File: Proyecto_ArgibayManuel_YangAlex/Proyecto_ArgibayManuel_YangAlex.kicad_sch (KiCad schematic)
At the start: 29 parts, among them J1 Con_1x3, J2 Con_1x2, J3 Con_1x3, J4 Conn_01x03_Pin, J5 Conn_01x06, SW1 SW_Push, SW2 SW_Push, SW3 SW_Push, SW4 SW_Push, U1 PIC18F258-I_SO, U2 HDC2010YPAR, U3 LT1716IS5TRMPBF, U4 LT1716IS5TRMPBF, U5 TXS0108EPW, Y1 Crystal

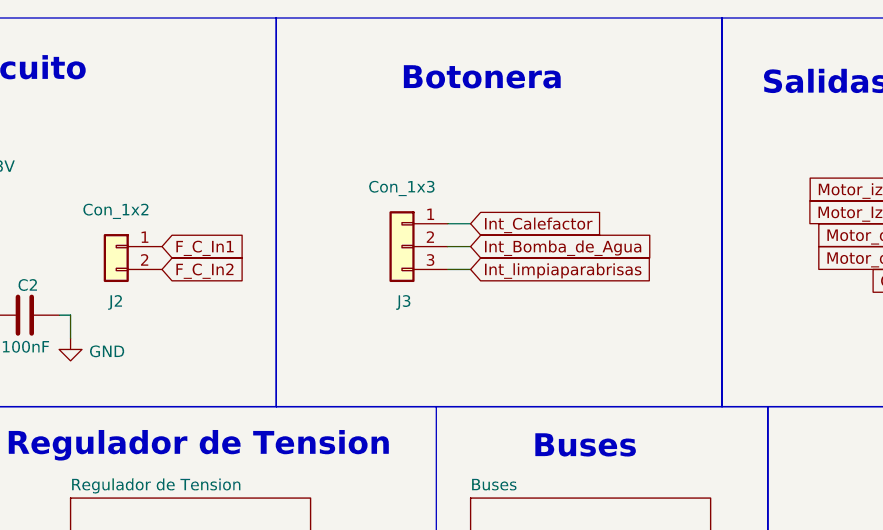
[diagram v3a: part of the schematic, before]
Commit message: Cambio layout (faltan agregar vías y reorganizar con la capa BOTTOM)
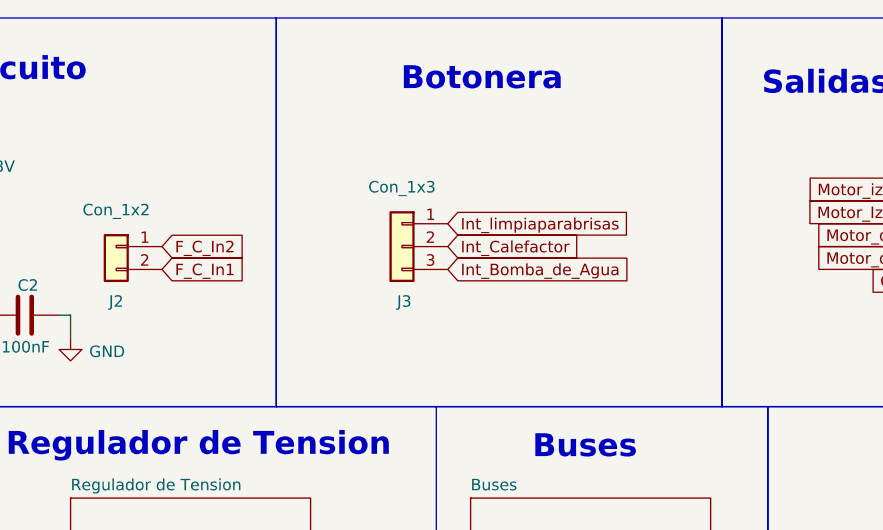
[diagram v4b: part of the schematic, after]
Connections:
- net F_C_In1: now also J2.2 (Pin_2); no longer J2.1 (Pin_1)
- net F_C_In2: now also J2.1 (Pin_1); no longer J2.2 (Pin_2)
- net Int_Bomba_de_Agua: now also J3.3 (Pin_3); no longer J3.2 (Pin_2)
- net Int_Calefactor: now also J3.2 (Pin_2); no longer J3.1 (Pin_1)
- net Int_limpiaparabrisas: now also J3.1 (Pin_1); no longer J3.3 (Pin_3)

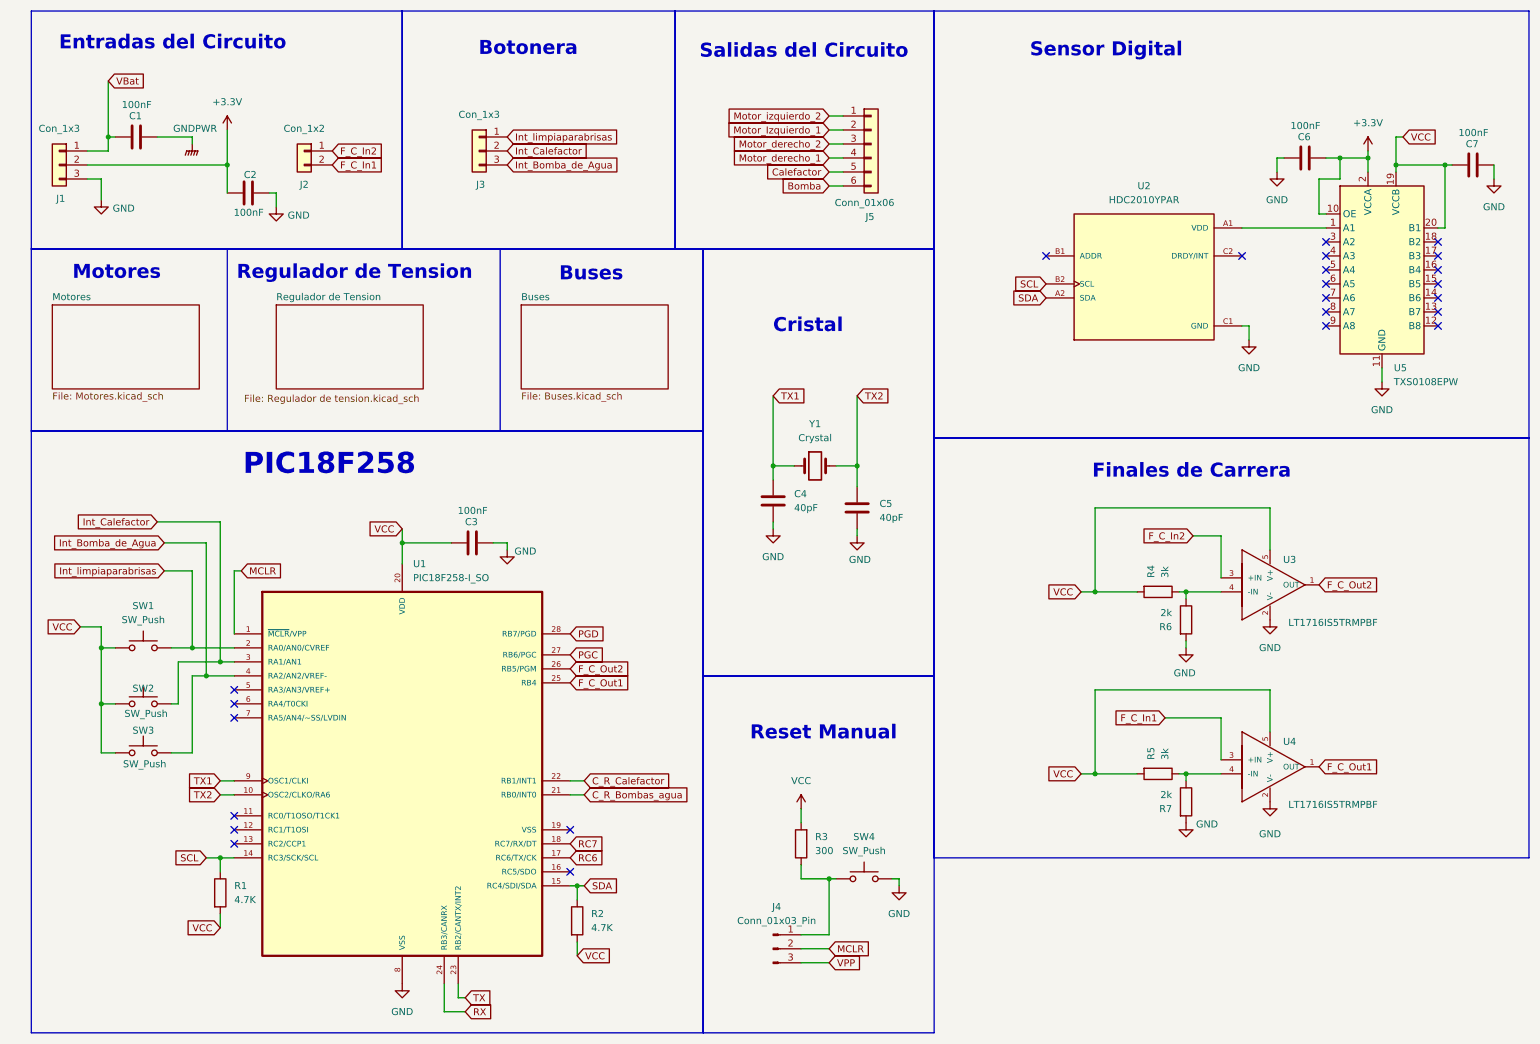
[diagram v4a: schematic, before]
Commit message: Termino layout (faltan acomodar etiquetas en la pcb))
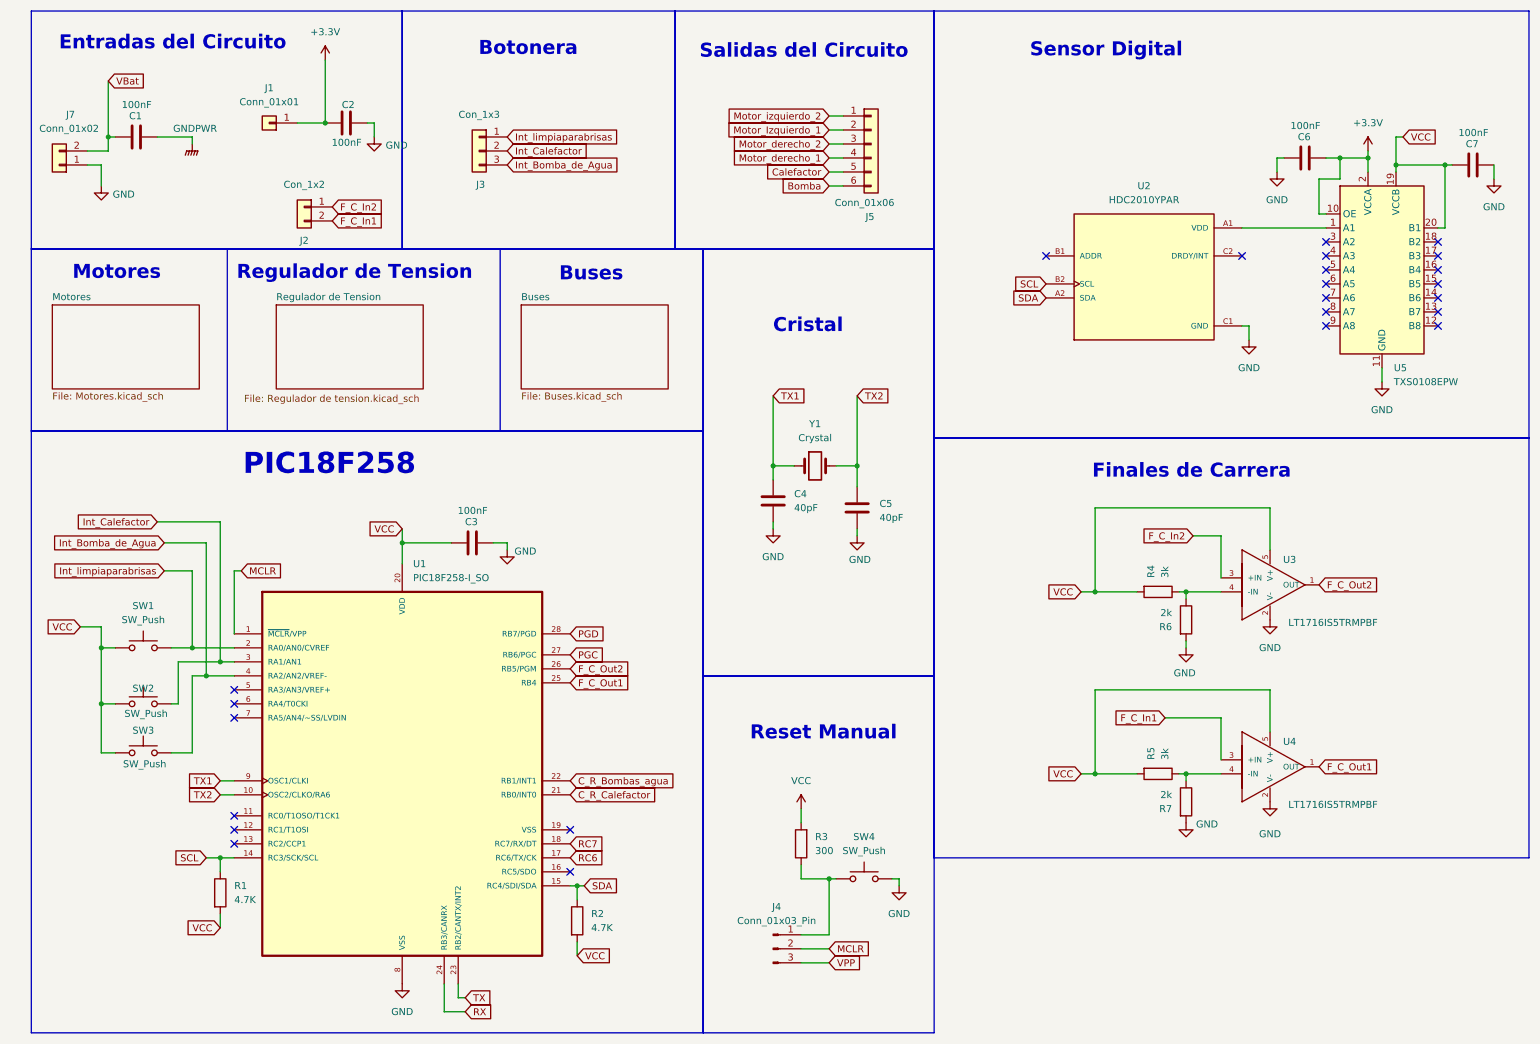
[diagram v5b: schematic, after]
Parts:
- removed J1: Con_1x3, Connector_PinHeader_2.54mm:PinHeader_1x03_P2.54mm_Vertical, symbol Connector_Generic:Conn_01x03
- added J1: Conn_01x01, Connector_PinHeader_2.54mm:PinHeader_1x01_P2.54mm_Vertical, symbol Connector_Generic:Conn_01x01
- added J7: Conn_01x02, Connector_PinHeader_2.54mm:PinHeader_1x02_P2.54mm_Vertical, symbol Connector_Generic:Conn_01x02
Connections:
- net +3.3V: now also J1.1 (Pin_1)
- net C_R_Bombas_agua: now also U1.22 (RB1/INT1); no longer U1.21 (RB0/INT0)
- net C_R_Calefactor: now also U1.21 (RB0/INT0); no longer U1.22 (RB1/INT1)
- net GND: now also J7.1 (Pin_1)
- net VBat: now also J7.2 (Pin_2)
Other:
- moved on the sheet: C2, J2

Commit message: Cambio de presentacion(esquematico,consumo,layout), minimas correciones en el esquematico
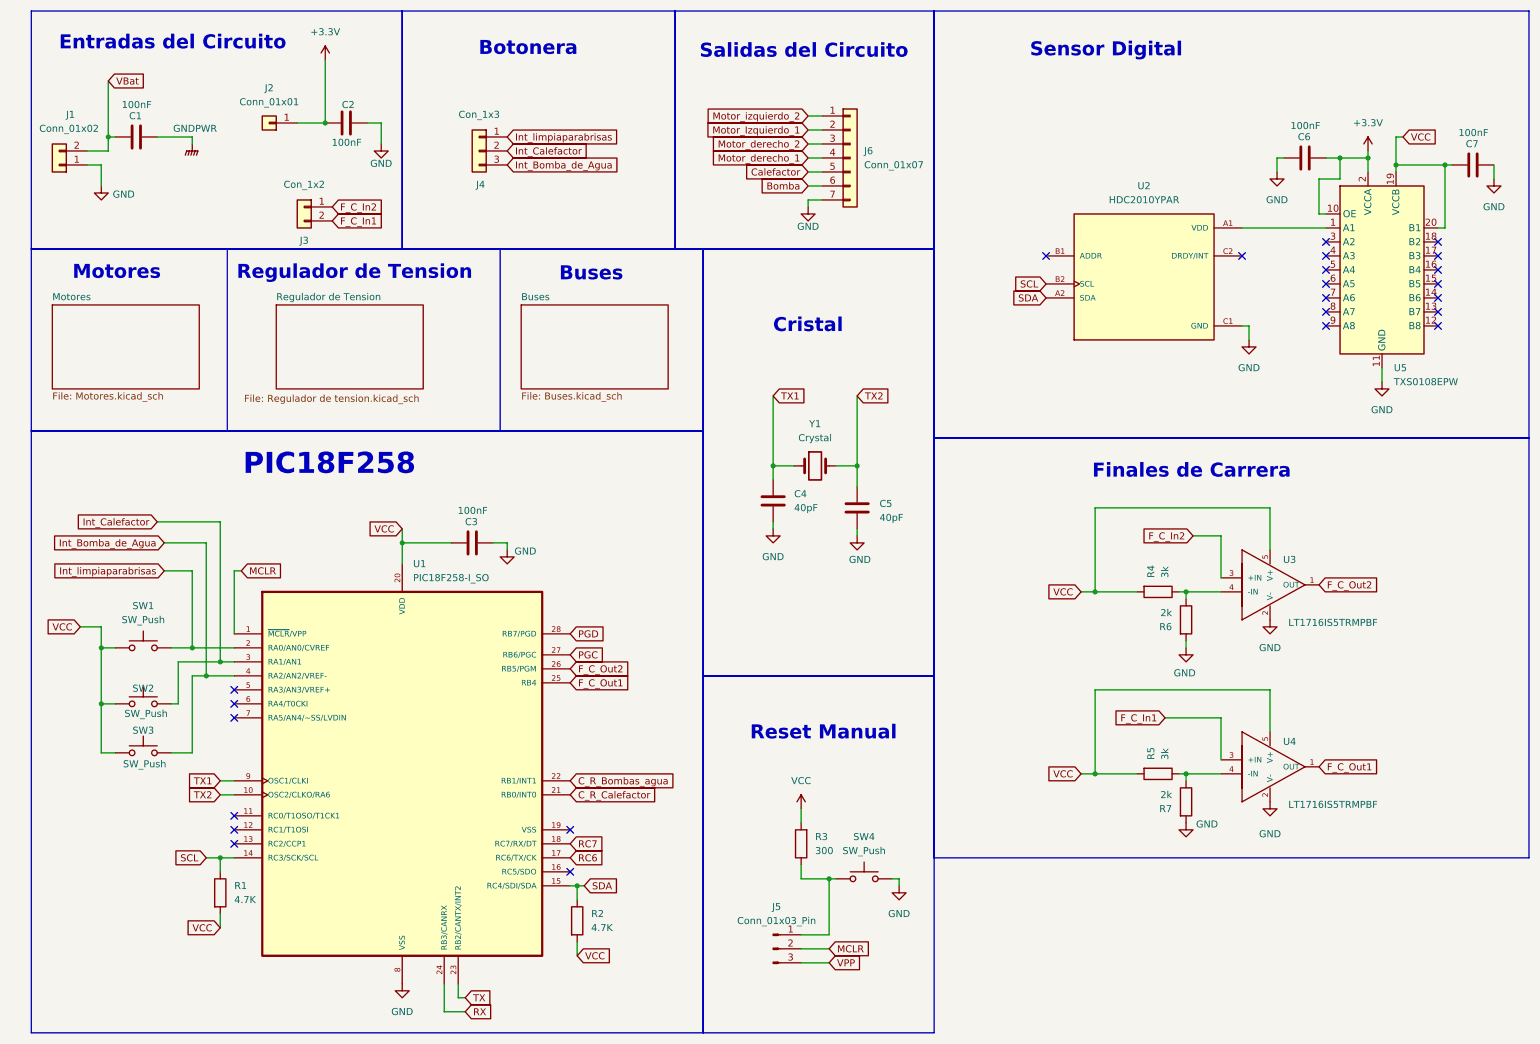
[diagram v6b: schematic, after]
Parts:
- removed J5: Conn_01x06, TerminalBlock_Phoenix:TerminalBlock_Phoenix_MKDS-1,5-6_1x06_P5.00mm_Horizontal, symbol Connector_Generic:Conn_01x06
- added J6: Conn_01x07, TerminalBlock_Phoenix:TerminalBlock_Phoenix_MKDS-1,5-7_1x07_P5.00mm_Horizontal, symbol Connector_Generic:Conn_01x07
- renumbered J7 to J1, J1 to J2, J2 to J3, J3 to J4, J4 to J5
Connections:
- net Bomba: now also J6.6 (Pin_6)
- net Calefactor: now also J6.5 (Pin_5)
- net GND: now also J6.7 (Pin_7)
- net Motor_Izquierdo_1: now also J6.2 (Pin_2)
- net Motor_derecho_1: now also J6.4 (Pin_4)
- net Motor_derecho_2: now also J6.3 (Pin_3)
- net Motor_izquierdo_2: now also J6.1 (Pin_1)

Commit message: Agrego cambios
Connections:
- net Bomba: now also J6.5 (Pin_5); no longer J6.6 (Pin_6)
- net Calefactor: now also J6.6 (Pin_6); no longer J6.5 (Pin_5)
- net GND: no longer J1.1 (Pin_1), J6.7 (Pin_7)
- net GNDPWR: now also J1.1 (Pin_1), J6.7 (Pin_7)
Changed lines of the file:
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@@
 	(wire
 		(pts
-			(xy 153.67 41.91) (xy 156.21 41.91)
+			(xy 260.35 35.56) (xy 260.35 40.64)
 		)
 		(stroke
@@
 		)
 	)
-	(wire
+	(polyline
 		(pts
-			(xy 260.35 35.56) (xy 260.35 40.64)
+			(xy 97.79 55.88) (xy 97.79 88.9)
 		)
 		(stroke
@@
 		)
 	)
-	(polyline
+	(wire
 		(pts
-			(xy 97.79 55.88) (xy 97.79 88.9)
+			(xy 153.67 41.91) (xy 156.21 41.91)
 		)
 		(stroke
@@
 	(wire
 		(pts
+			(xy 153.67 44.45) (xy 156.21 44.45)
+		)
+		(stroke
+			(width 0)
+			(type default)
+		)
+	)
+	(wire
+		(pts
 			(xy 44.45 133.35) (xy 49.53 133.35)
 		)
@@
 	(wire
 		(pts
-			(xy 153.67 44.45) (xy 156.21 44.45)
-		)
-		(stroke
-			(width 0)
-			(type default)
-		)
-	)
-	(wire
-		(pts
 			(xy 153.67 46.99) (xy 156.21 46.99)
 		)
@@
 	(global_label "Calefactor"
 		(shape input)
-		(at 153.67 41.91 180)
+		(at 153.67 44.45 180)
 		(fields_autoplaced yes)
 		(effects
@@
 		)
 		(property "Intersheetrefs" "${INTERSHEET_REFS}"
-			(at 140.8878 41.91 0)
+			(at 140.8878 44.45 0)
 			(effects
 				(font
@@
 	(global_label "Bomba"
 		(shape input)
-		(at 153.67 44.45 180)
+		(at 153.67 41.91 180)
 		(fields_autoplaced yes)
 		(effects
@@
 		)
 		(property "Intersheetrefs" "${INTERSHEET_REFS}"
-			(at 144.2745 44.45 0)
+			(at 144.2745 41.91 0)
 			(effects
 				(font
@@
 	)
 	(symbol
+		(lib_id "power:GNDPWR")
+		(at 25.4 44.45 0)
+		(unit 1)
+		(exclude_from_sim no)
+		(in_bom yes)
+		(on_board yes)
+		(dnp no)
+		(property "Reference" "#PWR039"
+			(at 25.4 49.53 0)
+			(effects
+				(font
+					(size 1.27 1.27)
+				)
+				(hide yes)
+			)
+		)
+		(property "Value" "GNDPWR"
+			(at 25.908 41.656 0)
+			(effects
+				(font
+					(size 1.27 1.27)
+				)
+			)
+		)
+		(property "Footprint" ""
+			(at 25.4 45.72 0)
+			(effects
+				(font
+					(size 1.27 1.27)
+				)
+				(hide yes)
+			)
+		)
+		(property "Datasheet" ""
+			(at 25.4 45.72 0)
+			(effects
+				(font
+					(size 1.27 1.27)
+				)
+				(hide yes)
+			)
+		)
+		(property "Description" "Power symbol creates a global label with name \"GNDPWR\" , global ground"
+			(at 25.4 44.45 0)
+			(effects
+				(font
+					(size 1.27 1.27)
+				)
+				(hide yes)
+			)
+		)
+		(pin "1"
+		)
+		(instances
+			(project "Proyecto_ArgibayManuel_YangAlex"
+				(path "/b2dde924-33f5-41ab-a1bf-811873450a89"
+					(reference "#PWR039")
+					(unit 1)
+				)
+			)
+		)
+	)
+	(symbol
 		(lib_id "power:GND")
 		(at 238.76 41.91 0)
@@
 	)
 	(symbol
-		(lib_id "power:GND")
-		(at 153.67 48.26 0)
-		(unit 1)
-		(exclude_from_sim no)
-		(in_bom yes)
-		(on_board yes)
-		(dnp no)
-		(property "Reference" "#PWR09"
-			(at 153.67 54.61 0)
-			(effects
-				(font
-					(size 1.27 1.27)
-				)
-				(hide yes)
-			)
-		)
-		(property "Value" "GND"
-			(at 153.67 51.816 0)
-			(effects
-				(font
-					(size 1.27 1.27)
-				)
-			)
-		)
-		(property "Footprint" ""
-			(at 153.67 48.26 0)
-			(effects
-				(font
-					(size 1.27 1.27)
-				)
-				(hide yes)
-			)
-		)
-		(property "Datasheet" ""
-			(at 153.67 48.26 0)
-			(effects
-				(font
-					(size 1.27 1.27)
-				)
-				(hide yes)
-			)
-		)
-		(property "Description" "Power symbol creates a global label with name \"GND\" , ground"
-			(at 153.67 48.26 0)
-			(effects
-				(font
-					(size 1.27 1.27)
-				)
-				(hide yes)
-			)
-		)
-		(pin "1"
-		)
-		(instances
-			(project "Proyecto_ArgibayManuel_YangAlex"
-				(path "/b2dde924-33f5-41ab-a1bf-811873450a89"
-					(reference "#PWR09")
-					(unit 1)
-				)
-			)
-		)
-	)
-	(symbol
 		(lib_id "Connector_Generic:Conn_01x03")
 		(at 93.98 38.1 0)
@@
 	(symbol
 		(lib_id "power:GND")
-		(at 25.4 44.45 0)
-		(unit 1)
-		(exclude_from_sim no)
-		(in_bom yes)
-		(on_board yes)
-		(dnp no)
-		(property "Reference" "#PWR01"
-			(at 25.4 50.8 0)
-			(effects
-				(font
-					(size 1.27 1.27)
-				)
-				(hide yes)
-			)
-		)
-		(property "Value" "GND"
-			(at 29.464 45.974 0)
-			(effects
-				(font
-					(size 1.27 1.27)
-				)
-			)
-		)
-		(property "Footprint" ""
-			(at 25.4 44.45 0)
-			(effects
-				(font
-					(size 1.27 1.27)
-				)
-				(hide yes)
-			)
-		)
-		(property "Datasheet" ""
-			(at 25.4 44.45 0)
-			(effects
-				(font
-					(size 1.27 1.27)
-				)
-				(hide yes)
-			)
-		)
-		(property "Description" "Power symbol creates a global label with name \"GND\" , ground"
-			(at 25.4 44.45 0)
-			(effects
-				(font
-					(size 1.27 1.27)
-				)
-				(hide yes)
-			)
-		)
-		(pin "1"
-		)
-		(instances
-			(project ""
-				(path "/b2dde924-33f5-41ab-a1bf-811873450a89"
-					(reference "#PWR01")
-					(unit 1)
-				)
-			)
-		)
-	)
-	(symbol
-		(lib_id "power:GND")
 		(at 222.25 160.02 0)
 		(unit 1)
@@
 					(unit 1)
 				)
+			)
+		)
+	)
+	(symbol
+		(lib_id "power:GNDPWR")
+		(at 153.67 48.26 0)
+		(unit 1)
+		(exclude_from_sim no)
+		(in_bom yes)
+		(on_board yes)
+		(dnp no)
+		(property "Reference" "#PWR09"
+			(at 153.67 53.34 0)
+			(effects
+				(font
+					(size 1.27 1.27)
+				)
+				(hide yes)
+			)
+		)
+		(property "Value" "GNDPWR"
+			(at 154.178 45.466 0)
+			(effects
+				(font
+					(size 1.27 1.27)
+				)
+			)
+		)
+		(property "Footprint" ""
+			(at 153.67 49.53 0)
+			(effects
+				(font
+					(size 1.27 1.27)
+				)
+				(hide yes)
+			)
+		)
+		(property "Datasheet" ""
+			(at 153.67 49.53 0)
+			(effects
+				(font
+					(size 1.27 1.27)
+				)
+				(hide yes)
+			)
+		)
+		(property "Description" "Power symbol creates a global label with name \"GNDPWR\" , global ground"
+			(at 153.67 48.26 0)
+			(effects
+				(font
+					(size 1.27 1.27)
+				)
+				(hide yes)
+			)
+		)
+		(pin "1"
+		)
+		(instances
+			(project "Proyecto_ArgibayManuel_YangAlex"
+				(path "/b2dde924-33f5-41ab-a1bf-811873450a89"
+					(reference "#PWR09")
+					(unit 1)
+				)

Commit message: Arreglo layout y esqumatico con las correcciones pasadas
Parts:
- C1, C2, C3, C6, C7: footprint Capacitor_THT:CP_Radial_D5.0mm_P2.00mm -> Capacitor_SMD:C_0805_2012Metric
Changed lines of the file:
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@@
 			)
 		)
-		(property "Footprint" "Capacitor_THT:CP_Radial_D5.0mm_P2.00mm"
+		(property "Footprint" "Capacitor_SMD:C_0805_2012Metric"
 			(at 247.65 38.4048 0)
 			(effects
@@
 			)
 		)
-		(property "Footprint" "Capacitor_THT:CP_Radial_D5.0mm_P2.00mm"
+		(property "Footprint" "Capacitor_SMD:C_0805_2012Metric"
 			(at 73.66 32.0548 0)
 			(effects
@@
 			)
 		)
-		(property "Footprint" "Capacitor_THT:CP_Radial_D5.0mm_P2.00mm"
+		(property "Footprint" "Capacitor_SMD:C_0805_2012Metric"
 			(at 96.52 108.2548 0)
 			(effects
@@
 			)
 		)
-		(property "Footprint" "Capacitor_THT:CP_Radial_D5.0mm_P2.00mm"
+		(property "Footprint" "Capacitor_SMD:C_0805_2012Metric"
 			(at 35.56 34.5948 0)
 			(effects
@@
 			)
 		)
-		(property "Footprint" "Capacitor_THT:CP_Radial_D5.0mm_P2.00mm"
+		(property "Footprint" "Capacitor_SMD:C_0805_2012Metric"
 			(at 278.13 39.6748 0)
 			(effects
